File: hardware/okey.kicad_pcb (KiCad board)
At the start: 2 copper layers, 102.9 x 82.6 mm, 34 parts, among them IC1 4094N, IC2 4094N, P1 ROW_JMP, P2 CONN_02X13, P3 CONN_02X03, P4 CONN_02X08, P5 CONN_02X03, P6 CONN_02X10, SW1 MX_D, SW10 MX_D, SW11 MX_D, SW12 MX_D, SW13 MX_D, SW2 MX_D, SW3 MX_D, SW4 MX_D, SW5 MX_D, SW6 MX_D, SW7 MX_D, SW8 MX_D, SW9 MX_D, U1 4053, U2 4024

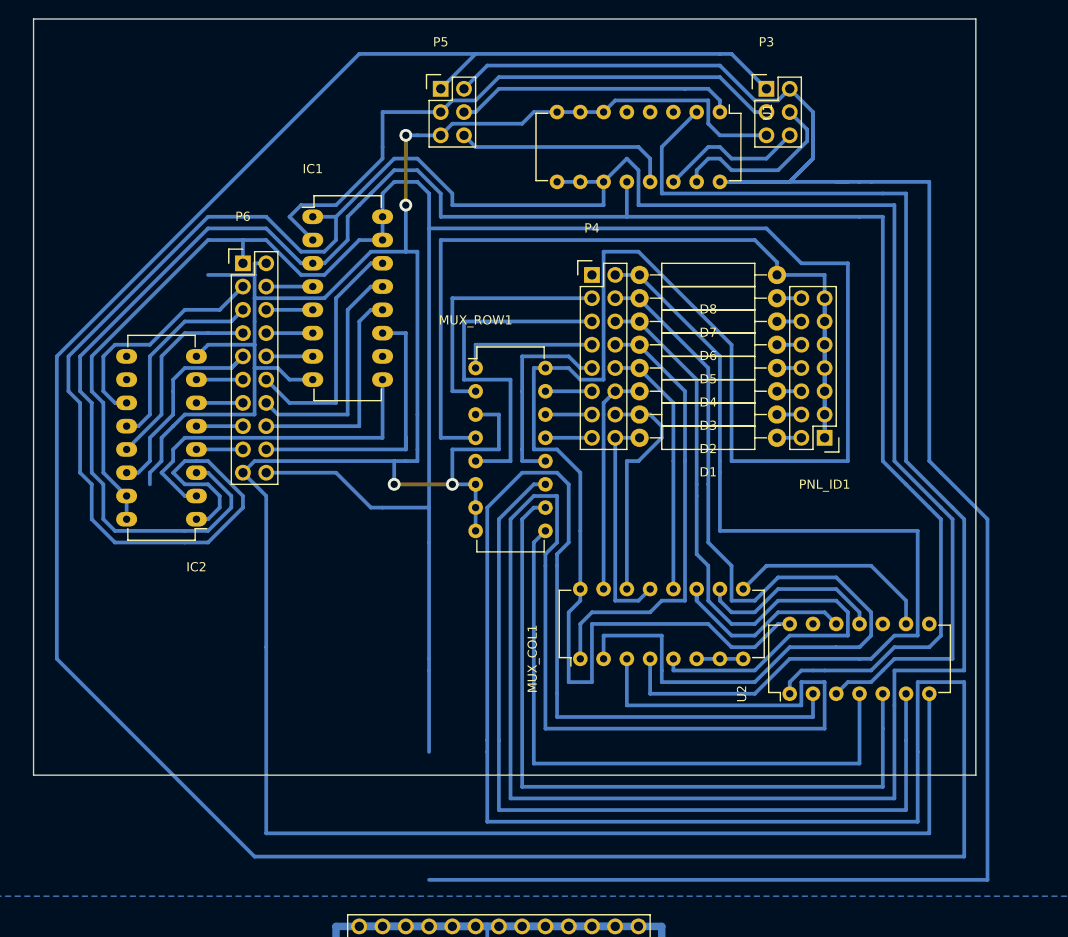
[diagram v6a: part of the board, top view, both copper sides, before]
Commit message: PCB: optimized routing
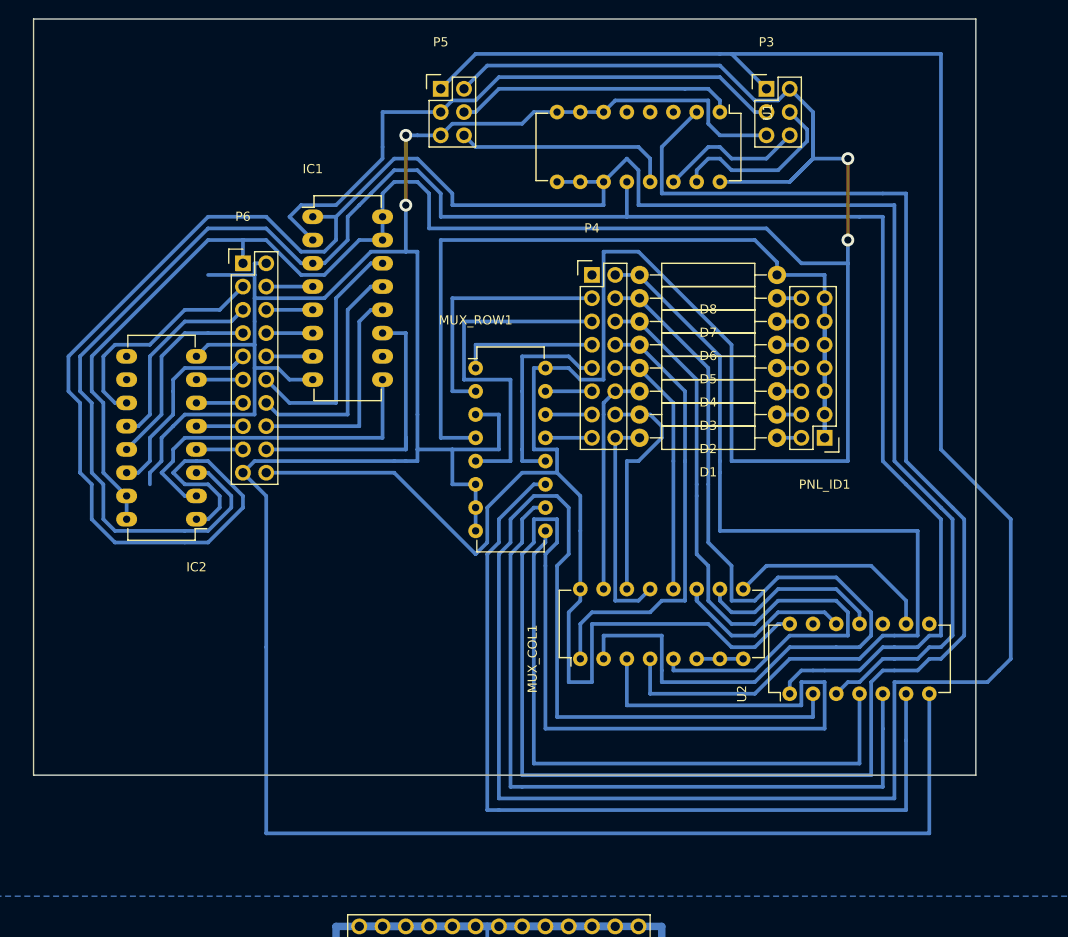
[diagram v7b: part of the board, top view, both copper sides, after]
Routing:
- net VDD: track 590.4 -> 406.5 mm, vias 0 -> 2
- net Net-(P3-Pad1): track 427.2 -> 293.2 mm
- net Net-(MUX_COL1-Pad3): track 282.6 -> 267.7 mm
- net GND: track 341.2 -> 336.1 mm, vias 4 -> 2
- net Net-(MUX_ROW1-Pad10): track 81.8 -> 83.6 mm
- net Net-(MUX_ROW1-Pad11): track 95.6 -> 97.4 mm
- net Net-(IC1-Pad1): track 248.0 -> 246.5 mm

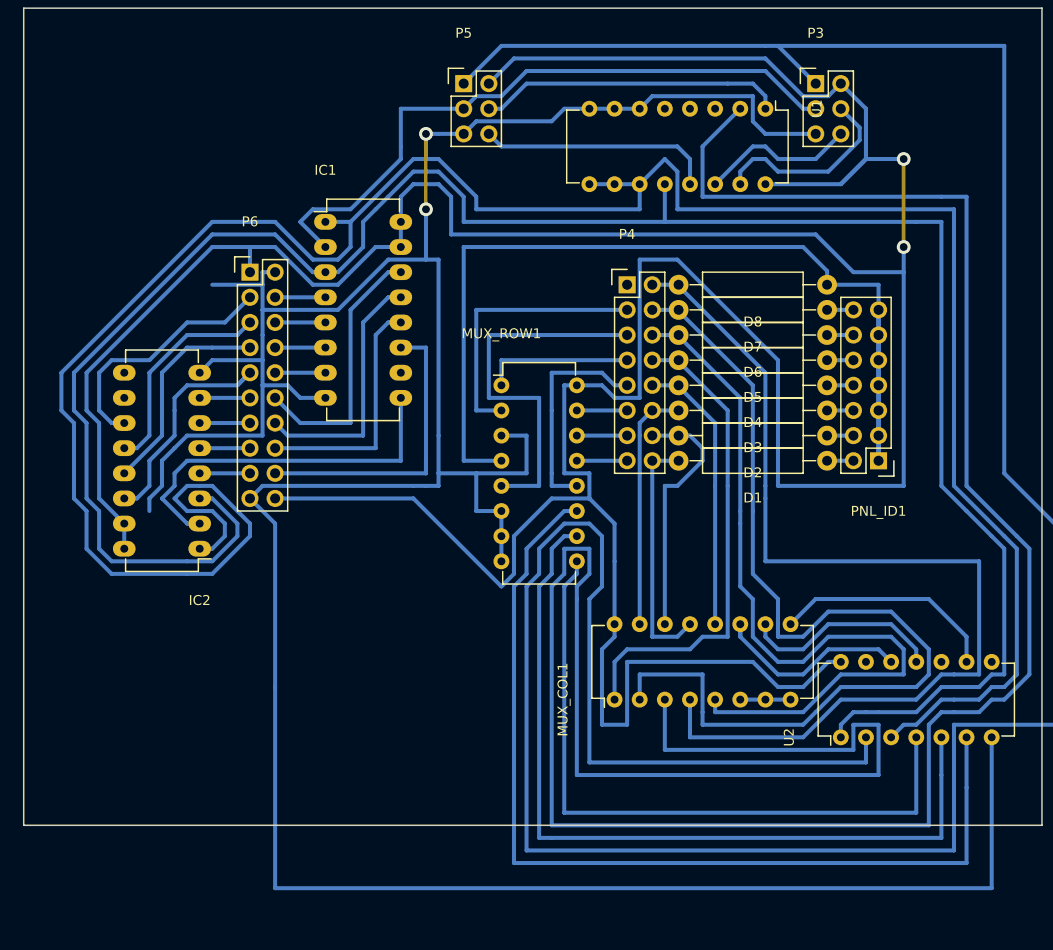
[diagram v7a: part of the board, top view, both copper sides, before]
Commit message: PCB: optimize routing
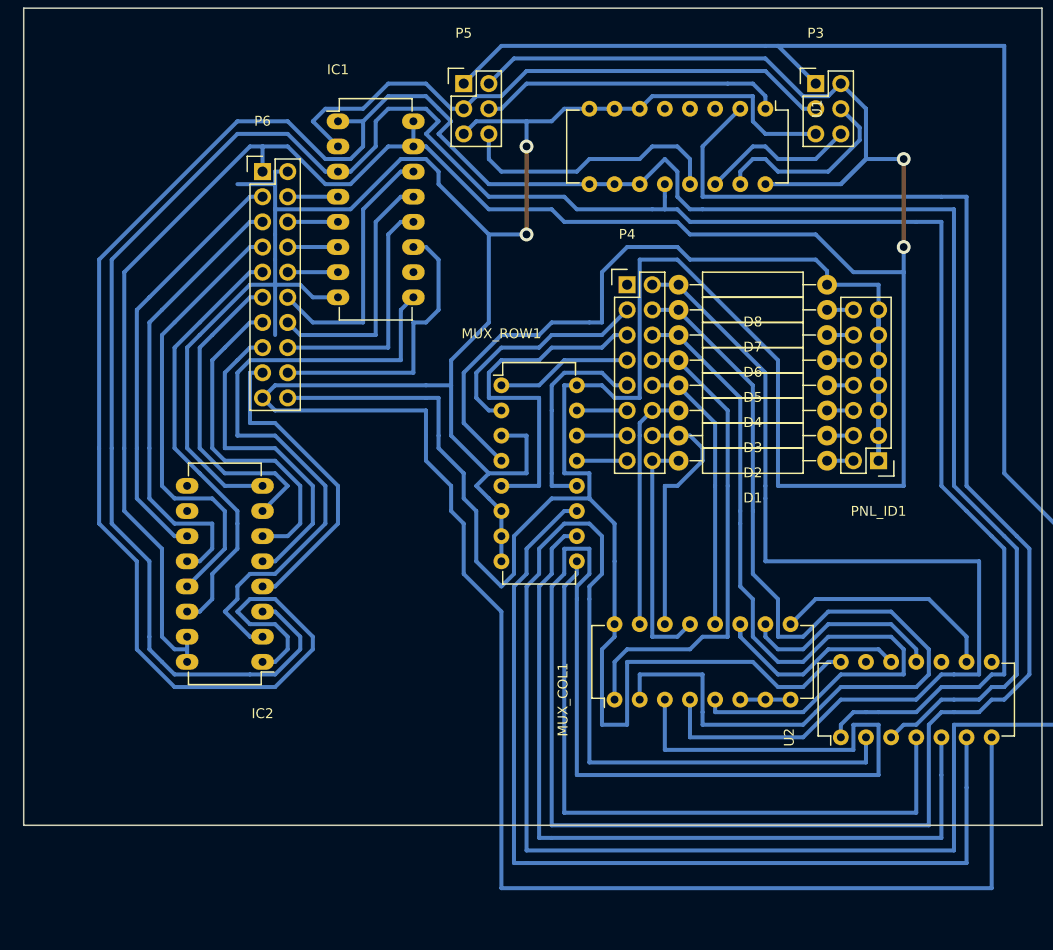
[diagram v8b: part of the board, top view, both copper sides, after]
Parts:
- moved IC2 13.1 mm to (111.8, 81.3)
- moved P6 10.2 mm to (111.8, 31.8)
- moved IC1 10.2 mm to (119.4, 26.7)
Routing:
- net Net-(IC2-Pad6): track 5.08 -> 34.2 mm
- net Net-(IC2-Pad5): track 5.08 -> 33.4 mm
- net Net-(IC2-Pad7): track 5.08 -> 32.7 mm
- net VDD: track 406.5 -> 434.0 mm
- net Net-(IC2-Pad4): track 5.08 -> 31.9 mm
- net Net-(IC1-Pad9): track 37.7 -> 64.5 mm
- net Net-(IC2-Pad12): track 21.7 -> 46.4 mm
- net Net-(IC2-Pad13): track 21.7 -> 45.7 mm
- net Net-(IC2-Pad14): track 23.5 -> 44.2 mm
- net Net-(IC1-Pad3): track 216.8 -> 237.3 mm
- net Net-(IC2-Pad11): track 25.3 -> 43.1 mm
- net Net-(IC1-Pad1): track 246.5 -> 259.5 mm
- net GND: track 336.1 -> 348.2 mm
- net Net-(D8-Pad1): track 102.7 -> 96.0 mm
- net Net-(IC1-Pad2): track 66.5 -> 60.2 mm
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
